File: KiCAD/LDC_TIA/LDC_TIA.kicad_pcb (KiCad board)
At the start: 2 copper layers, 22 parts, among them J1 Conn_01x02_Pin, J3 54-00166, J5 Conn_01x07_Pin, Q1 BC817, SW1 SW_SPST, U1 OPA2197xDGK, U2 LM7805_TO220, U4 LTC1044

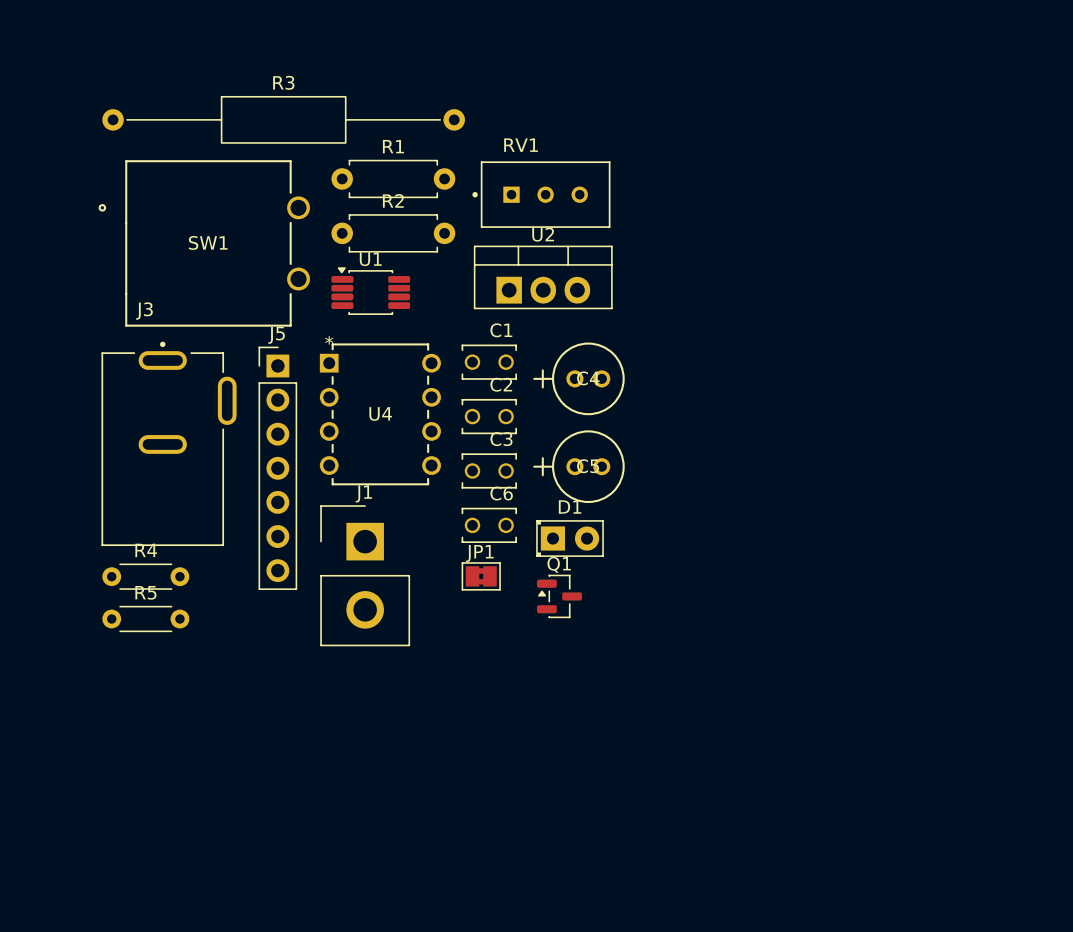
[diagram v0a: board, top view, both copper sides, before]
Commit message: updated schamatics in PCB
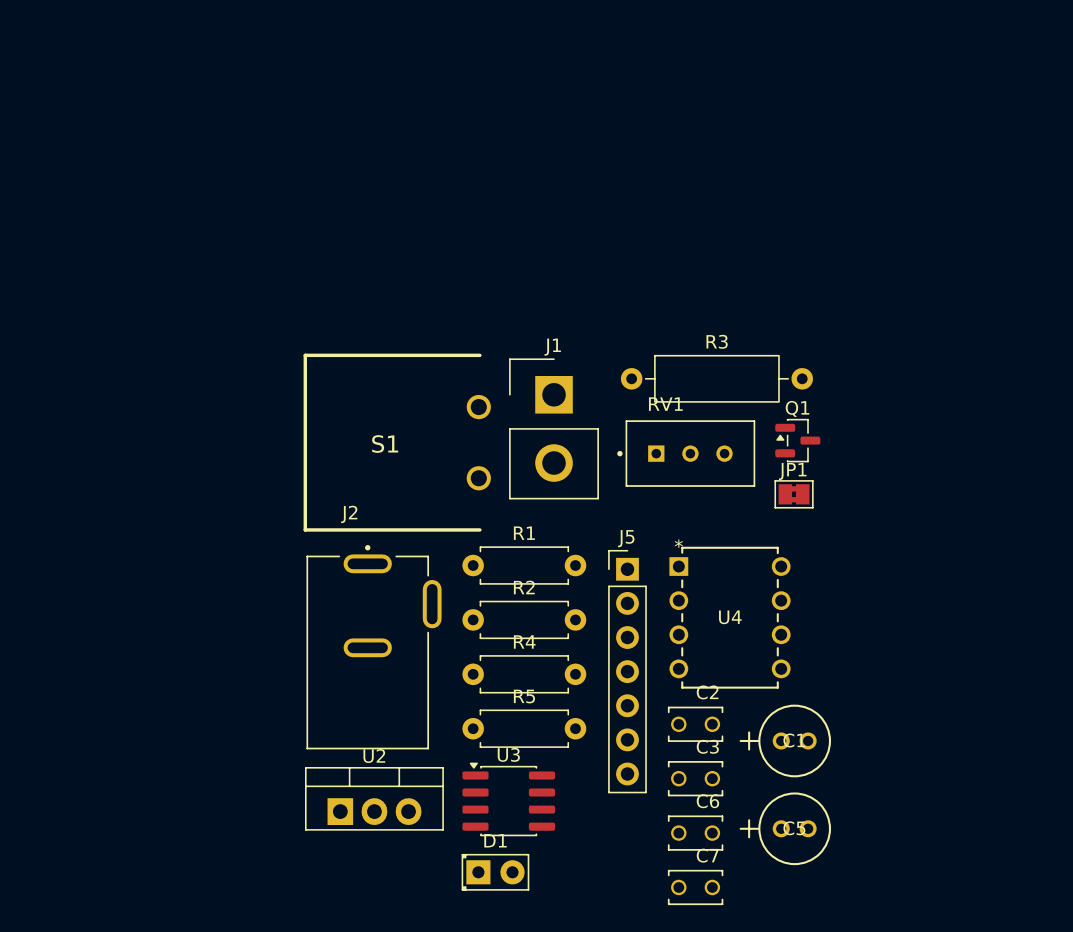
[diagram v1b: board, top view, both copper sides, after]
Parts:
- removed C4: 0.33uF, FOOTPRINTS:CAP_UEP_5X11_NCH
- removed J3: 54-00166, FOOTPRINTS:TENSILITY_54-00166
- removed SW1: SW_SPST, FOOTPRINTS:SWITCH_03211B
- removed U1: OPA2197xDGK, Package_SO:VSSOP-8_3x3mm_P0.65mm
- added C7: 10pF, FOOTPRINTS:CAPRB250W50L400T250H550, F.Cu at (158.8, 120.7)
- added J2: 54-00166, FOOTPRINTS:TENSILITY_54-00166, F.Cu at (134.4, 102.9)
- added S1: GPTS203211B, FOOTPRINTS:GPTS203211B, F.Cu at (142.7, 87.6)
- added U3: OPA2197xD, Package_SO:SOIC-8_3.9x4.9mm_P1.27mm, F.Cu at (144.9, 114.3)
- C1: value 10pF -> 0.1UF; footprint FOOTPRINTS:CAPRB250W50L400T250H550 -> FOOTPRINTS:CAP_UEP_5X11_NCH
- C5: value 0.1uF -> 0.33uF
- R1: value 2K -> 2k
- R2: value 1K -> 1k
- R3: footprint Resistor_THT:R_Axial_DIN0309_L9.0mm_D3.2mm_P25.40mm_Horizontal -> Resistor_THT:R_Axial_DIN0309_L9.0mm_D3.2mm_P12.70mm_Horizontal
- R4, R5: value 2k -> 2K; footprint Resistor_THT:R_Axial_DIN0204_L3.6mm_D1.6mm_P5.08mm_Horizontal -> Resistor_THT:R_Axial_DIN0207_L6.3mm_D2.5mm_P7.62mm_Horizontal
- moved R3 43.2 mm to (154.0, 82.9)
- moved U2 40.8 mm to (132.3, 115.1)
- moved C1 35.6 mm to (165.2, 109.8)
- moved C5 31.0 mm to (165.2, 116.4)
- moved R1 30.4 mm to (142.2, 96.8)
- moved R2 30.4 mm to (142.2, 100.8)
- moved U4 30.1 mm to (157.5, 96.8)
- moved J5 30.1 mm to (153.7, 97.0)
- moved R5 28.1 mm to (142.2, 108.9)
- moved R4 27.9 mm to (142.2, 104.9)
- moved C2 27.6 mm to (158.8, 108.6)
- moved C3 27.6 mm to (158.8, 112.6)
- moved C6 27.6 mm to (158.8, 116.7)
- moved D1 25.5 mm to (142.6, 119.6)
- moved JP1 24.1 mm to (166.1, 91.5)
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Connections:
- C1 pad 1: Net-(U1B-+) -> /+VCC
- C5 pad 1: /+VCC -> /VI
- R4 pad 1: Net-(U1B-+) -> Net-(U3B-+)

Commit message: PCB layout
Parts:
- removed C6: 10pF, FOOTPRINTS:CAPRB250W50L400T250H550
- J3: renamed from J1; footprint Connector_Samtec_HPM_THT:Samtec_HPM-02-01-x-S_Straight_1x02_Pitch5.08mm -> Connector_PinHeader_2.54mm:PinHeader_1x02_P2.54mm_Vertical
- moved C1 39.4 mm to (131.6, 92.2), turned to 90 degrees
- moved D1 33.3 mm to (131.6, 88.2), turned to 90 degrees
- moved C2 28.2 mm to (131.8, 100.5), turned to 90 degrees
- moved U3 20.0 mm to (150.1, 105.9)
- moved U1 19.6 mm to (152.8, 96.4)
- moved U2 19.5 mm to (138.0, 95.8)
- moved Q1 19.5 mm to (146.9, 86.3), turned to 180 degrees
- moved C3 17.2 mm to (149.0, 110.7)
- moved J2 16.4 mm to (163.3, 110.3), turned to 180 degrees
- moved J3 16.3 mm to (163.4, 90.0), turned to 180 degrees
- moved S1 15.1 mm to (128.1, 91.7)
- moved C4 14.3 mm to (145.5, 107.4), turned to -90 degrees
- moved R1 13.9 mm to (135.1, 92.9), turned to 90 degrees
- moved R5 12.4 mm to (145.3, 91.7)
- moved J1 12.1 mm to (122.5, 105.2), turned to -90 degrees
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- renumbered C7 to C1, C5 to C3, C3 to C4, C1 to C5, J2 to J1, J5 to J2, R4 to R1, R5 to R2, R1 to R3, R2 to R4, R3 to R5, U3 to U1, U4 to U2, U2 to U3
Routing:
- net GND: track 0.00 -> 129.7 mm, vias 0 -> 4
- net /+VCC: track 0.00 -> 99.2 mm, vias 0 -> 2
- net Net-(U1A-+): track 0.00 -> 55.4 mm, vias 0 -> 3
- net Net-(U1B-+): track 0.00 -> 48.1 mm, vias 0 -> 2
- net /CATHODE: track 0.00 -> 46.2 mm, vias 0 -> 2
- net /VOUT: track 0.00 -> 38.2 mm
- net /-VCC: track 0.00 -> 30.5 mm, vias 0 -> 2
- net Net-(U1A--): track 0.00 -> 28.0 mm, vias 0 -> 2
- net /VI: track 0.00 -> 27.8 mm, vias 0 -> 2
- net Net-(D1-K): track 0.00 -> 24.5 mm
- net Net-(J3-Pin_2): track 0.00 -> 19.7 mm
- net /ANODE: track 0.00 -> 13.4 mm
- net Net-(Q1-E): track 0.00 -> 12.2 mm
- net Net-(U2-CAP+): track 0.00 -> 10.9 mm
- net Net-(U2-CAP-): track 0.00 -> 9.61 mm
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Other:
- board outline added: 53.4 x 32.2 mm

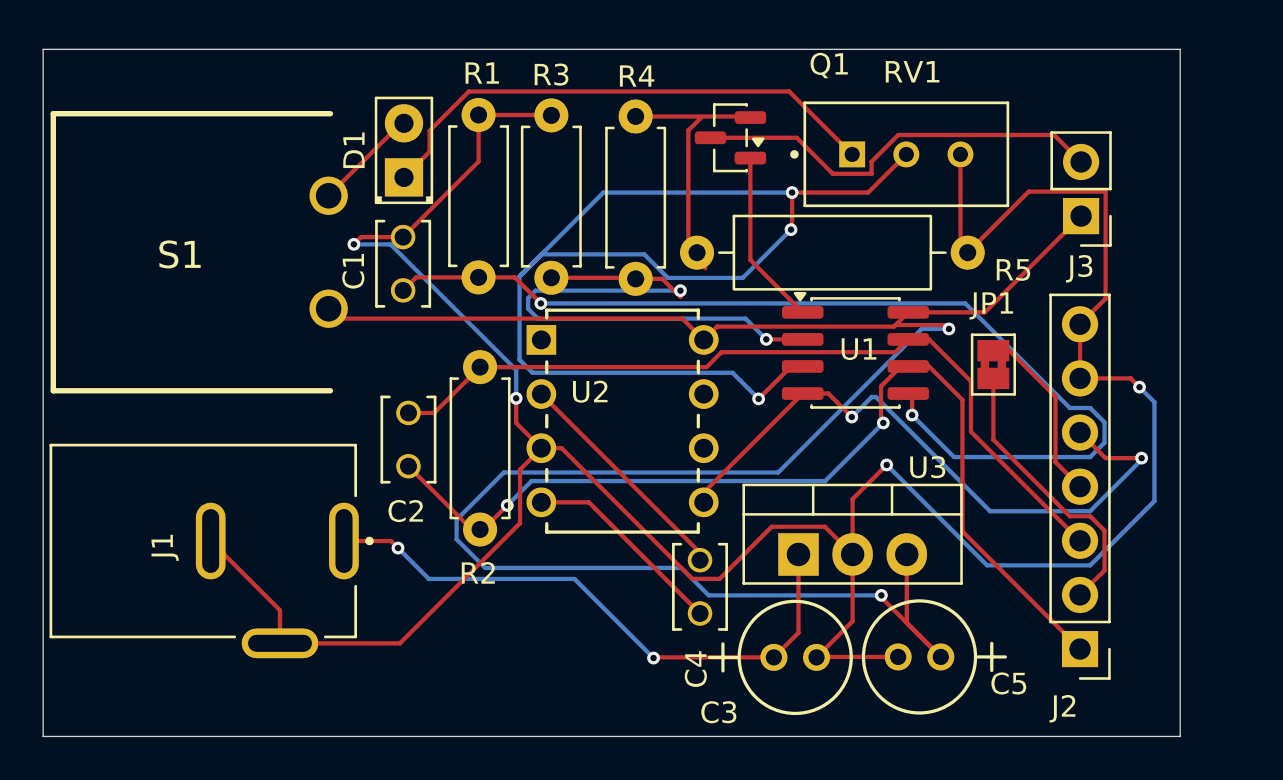
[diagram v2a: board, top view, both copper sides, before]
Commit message: PCB design and 3D Visualization
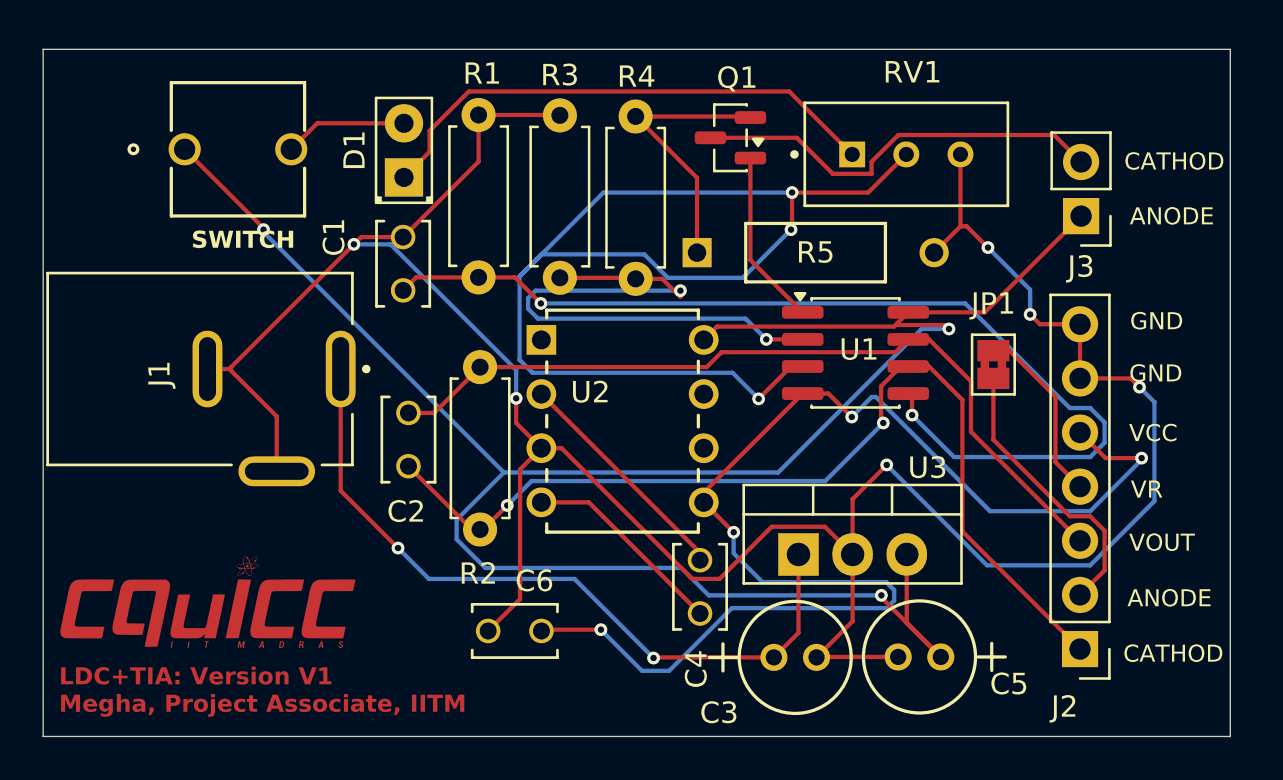
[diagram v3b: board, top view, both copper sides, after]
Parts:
- removed S1: GPTS203211B, FOOTPRINTS:GPTS203211B
- added C6: 10pF, FOOTPRINTS:CAPRB250W50L400T250H550, F.Cu at (136.8, 109.5)
- added G***: LOGO, LOGO, F.Cu at (122.4, 108.2)
- added SW1: B3F-6020, FOOTPRINTS:SW_B3F-6020_OMR, F.Cu at (121.3, 86.8)
- R5: footprint Resistor_THT:R_Axial_DIN0309_L9.0mm_D3.2mm_P12.70mm_Horizontal -> FOOTPRINTS:RES_MRS25_VIS
- moved J1 8.07 mm to (122.4, 97.2)
- moved R3 0.40 mm to (138.9, 92.9)
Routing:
- net /-VCC: track 30.5 -> 60.9 mm, vias 2 -> 4
- net /VI: track 27.8 -> 34.6 mm
- net GND: track 129.7 -> 124.9 mm, vias 4 -> 6
- net /+VCC: track 99.2 -> 102.3 mm, vias 2 -> 3
- net Net-(Q1-E): track 12.2 -> 13.5 mm
- net Net-(D1-A): track 4.94 -> 5.80 mm
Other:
- board size 53.4 x 32.2 mm -> 55.7 x 32.2 mm
- board text added: "ANODE"
- board text added: "CATHOD"
- board text added: "GND"
- board text added: "LDC+TIA: Version V1 Megha, Project Associate, IITM"
- board text added: "SWITCH"
- board text added: "VCC"
- board text added: "VOUT"
- board text added: "VR"

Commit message: PCB VOL 2
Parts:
- moved C5 48.1 mm to (130.8, 70.2), turned to 90 degrees
- moved U3 46.6 mm to (129.8, 63.9)
- moved C3 44.3 mm to (142.4, 66.8)
- moved C4 36.4 mm to (135.4, 72.4), turned to 180 degrees
- moved C6 35.4 mm to (150.3, 76.7), turned to 180 degrees
- moved J3 31.5 mm to (133.8, 101.0), turned to -90 degrees
- moved D1 30.1 mm to (144.9, 61.2), turned to 180 degrees
- moved J1 24.9 mm to (119.9, 72.4)
- moved SW1 24.8 mm to (115.5, 62.7)
- moved R4 24.8 mm to (119.3, 84.2), turned to -90 degrees
- moved Q1 23.1 mm to (126.6, 97.3), turned to -90 degrees
- moved R5 22.1 mm to (123.3, 93.3), turned to 90 degrees
- moved RV1 19.8 mm to (152.5, 67.5)
- moved U2 19.4 mm to (144.2, 77.4), turned to -90 degrees
- moved J2 19.0 mm to (148.5, 98.5)
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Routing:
- net /VOUT: track 38.2 -> 70.4 mm
- net /-VCC: track 60.9 -> 31.9 mm, vias 4 -> 0
- net Net-(U1B-+): track 48.1 -> 26.9 mm, vias 2 -> 0
- net GND: track 124.9 -> 105.1 mm, vias 6 -> 0
- net Net-(D1-A): track 5.80 -> 22.5 mm
- net Net-(D1-K): track 24.5 -> 8.44 mm
- net Net-(U1A--): track 28.0 -> 42.9 mm, vias 2 -> 0
- net Net-(J3-Pin_2): track 19.7 -> 5.88 mm
- net /+VCC: track 102.3 -> 91.3 mm, vias 3 -> 1
- net /VI: track 34.6 -> 24.8 mm, vias 2 -> 0
- net /CATHODE: track 46.2 -> 38.8 mm
- net Net-(Q1-E): track 13.5 -> 8.60 mm
- net Net-(U2-CAP+): track 10.9 -> 7.12 mm
- net /VR: track 8.50 -> 4.82 mm
- net /ANODE: track 13.4 -> 9.78 mm
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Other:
- board size 55.7 x 32.2 mm -> 57.3 x 58 mm
- board text removed: "ANODE"
- board text removed: "CATHOD"
- board text removed: "GND"
- board text removed: "SWITCH"
- board text removed: "VCC"
- board text removed: "VOUT"
- board text removed: "VR"

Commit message: PCB_LAYOUT_VOL2
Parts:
- removed SW1: B3F-6020, FOOTPRINTS:SW_B3F-6020_OMR
- added SW2: B3F-6020, FOOTPRINTS:SW_B3F-6020_OMR, F.Cu at (150.4, 96.8)
- moved C1 57.3 mm to (165.0, 113.6), turned to -90 degrees
- moved R4 56.1 mm to (171.8, 104.0), turned to 180 degrees
- moved R5 48.7 mm to (171.8, 97.5), turned to 180 degrees
- moved R1 48.0 mm to (165.4, 117.8), turned to 180 degrees
- moved C4 47.8 mm to (149.8, 118.0)
- moved C2 47.1 mm to (171.5, 109.8), turned to 90 degrees
- moved R3 46.4 mm to (171.8, 100.8), turned to 180 degrees
- moved JP1 45.3 mm to (183.8, 112.2)
- moved RV1 43.6 mm to (155.8, 111.0), turned to -90 degrees
- moved U3 42.4 mm to (145.9, 103.1)
- moved C5 41.7 mm to (156.7, 102.7)
- moved J3 41.6 mm to (175.4, 98.0), turned to 180 degrees
- moved R2 41.0 mm to (168.3, 116.2), turned to 90 degrees
- moved C6 38.2 mm to (160.3, 113.6), turned to 90 degrees
- moved J1 36.8 mm to (135.3, 105.8)
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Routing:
- net /VOUT: track 70.4 -> 11.8 mm
- net Net-(U1A-+): track 53.1 -> 5.35 mm
- net /+VCC: track 91.3 -> 55.4 mm, vias 1 -> 0
- net GND: track 105.1 -> 132.9 mm
- net Net-(U1A--): track 42.9 -> 16.2 mm
- net Net-(D1-K): track 8.44 -> 28.0 mm
- net Net-(U1B-+): track 26.9 -> 8.19 mm
- net /CATHODE: track 38.8 -> 21.0 mm, vias 2 -> 0
- net Net-(D1-A): track 22.5 -> 6.23 mm
- net Net-(J3-Pin_2): track 5.88 -> 17.1 mm
- net /ANODE: track 9.78 -> 0.00 mm
- net Net-(Q1-B): track 10.2 -> 2.02 mm
- net /-VCC: track 31.9 -> 39.1 mm
- net /VR: track 4.82 -> 0.00 mm
- net Net-(U2-CAP+): track 7.12 -> 11.3 mm
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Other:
- board outline removed
- board text added: "-VCC"
- board text added: "ANODE"
- board text added: "CATHOD"
- board text added: "GND"
- board text added: "VOUT"
- board text added: "VR"
